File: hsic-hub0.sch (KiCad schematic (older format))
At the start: 26 parts

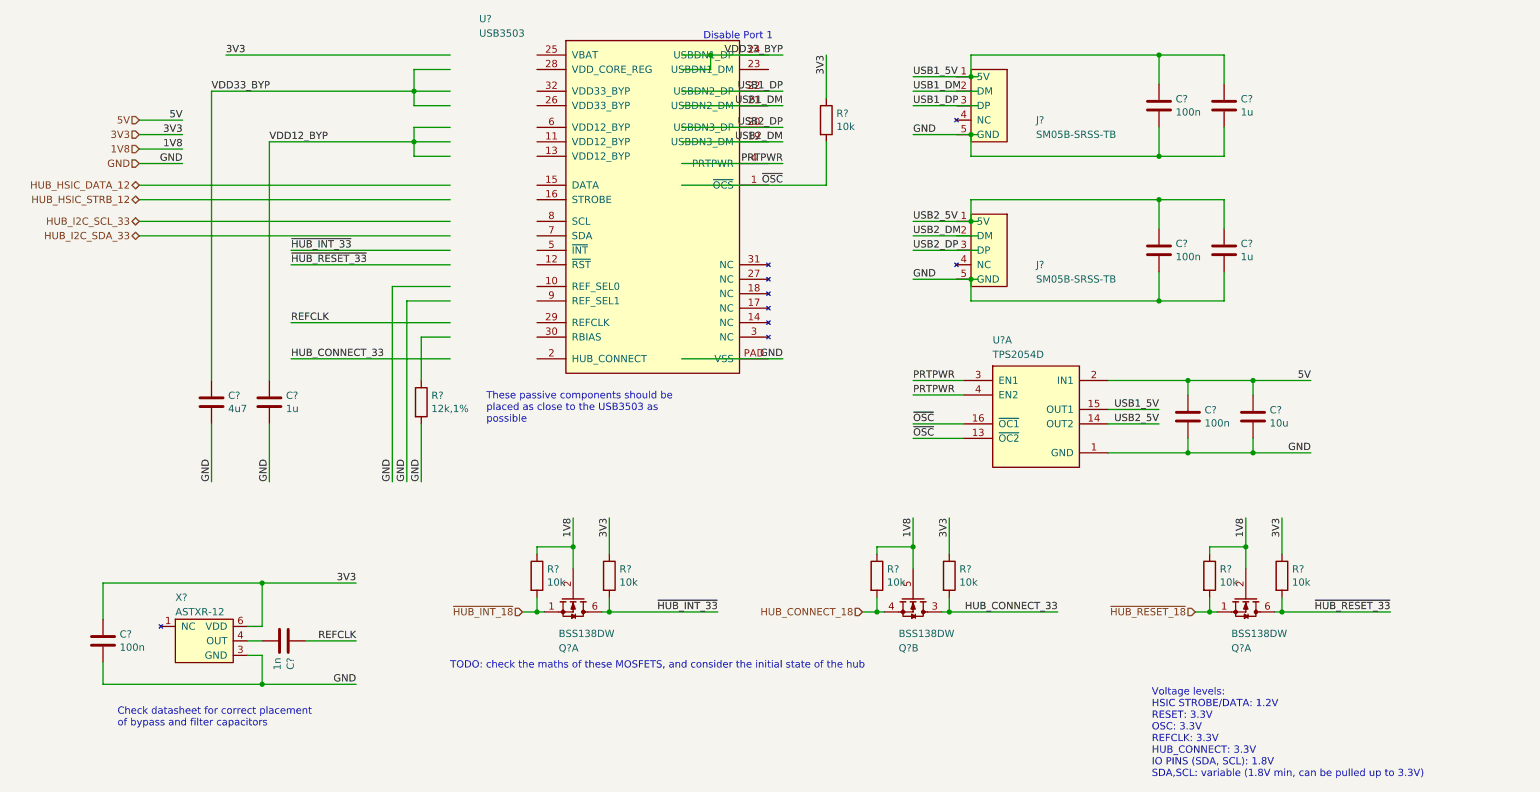
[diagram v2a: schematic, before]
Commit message: Added GPIO expander for hub signals.
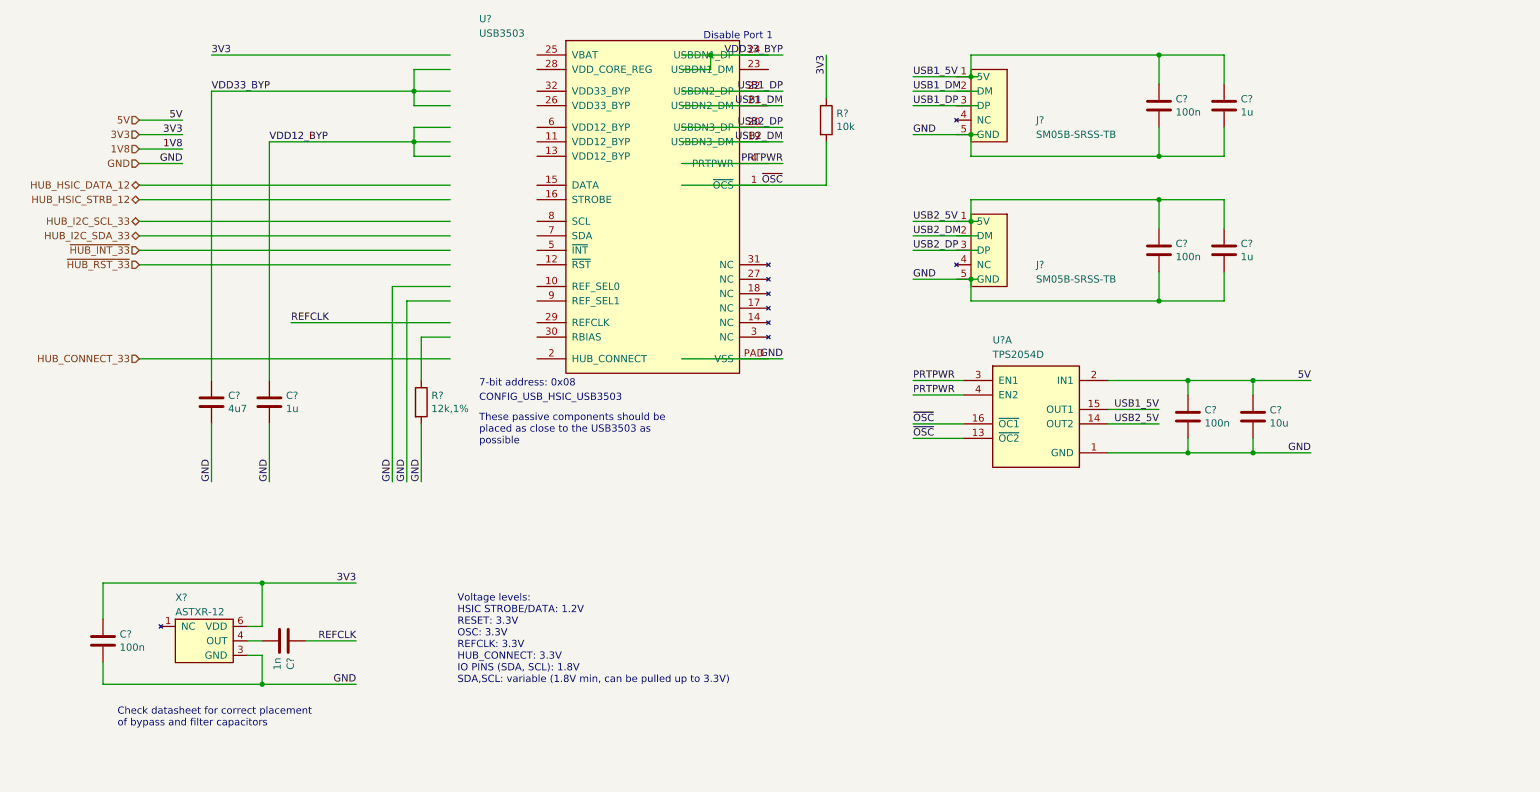
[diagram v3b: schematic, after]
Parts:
- removed Q? (x3): BSS138DW, symbol Drone:BSS138DW
- removed R? (x6): 10k, symbol Device:R
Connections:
- net labels added: ~HUB_RST_33
- net labels removed: HUB_CONNECT_18, ~HUB_INT_18, ~HUB_RESET_18, ~HUB_RESET_33
- wire segments 142 -> 109
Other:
- note added: "7-bit address: 0x08"
- note added: "CONFIG_USB_HSIC_USB3503"
- note removed: "TODO: check the maths of these MOSFETS, and consider the initial state of the hub"

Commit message: Use 0805 for all capacitors and resistors.
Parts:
- C? (x10): footprint (none) -> Capacitor_SMD:C_0805_2012Metric_Pad1.15x1.40mm_HandSolder; symbol Device:C -> Drone:CAP
- R? (x2): footprint (none) -> Resistor_SMD:R_0805_2012Metric_Pad1.15x1.40mm_HandSolder; symbol Device:R -> Drone:RES
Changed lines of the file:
@@
 	1400 2300 3550 2300
 $Comp
-L Device:C C?
+L Drone:CAP C?
 U 1 1 5E328065
 P 1150 5000
@@
 F 0 "C?" H 1265 5046 50  0000 L CNN
 F 1 "100n" H 1265 4955 50  0000 L CNN
-F 2 "" H 1188 4850 50  0001 C CNN
+F 2 "Capacitor_SMD:C_0805_2012Metric_Pad1.15x1.40mm_HandSolder" H 1188 4850 50  0001 C CNN
 F 3 "~" H 1150 5000 50  0001 C CNN
 	1    1150 5000
@@
 	5150 1700 5850 1700
 $Comp
-L Device:C C?
+L Drone:CAP C?
 U 1 1 5E332CF8
 P 8650 3450
@@
 F 0 "C?" H 8765 3496 50  0000 L CNN
 F 1 "100n" H 8765 3405 50  0000 L CNN
-F 2 "" H 8688 3300 50  0001 C CNN
+F 2 "Capacitor_SMD:C_0805_2012Metric_Pad1.15x1.40mm_HandSolder" H 8688 3300 50  0001 C CNN
 F 3 "~" H 8650 3450 50  0001 C CNN
 	1    8650 3450
@@
 	3150 2550 3550 2550
 $Comp
-L Device:C C?
+L Drone:CAP C?
 U 1 1 5E338829
 P 2400 5000
@@
 F 0 "C?" H 2515 5046 50  0000 L CNN
 F 1 "1n" H 2515 4955 50  0000 L CNN
-F 2 "" H 2438 4850 50  0001 C CNN
+F 2 "Capacitor_SMD:C_0805_2012Metric_Pad1.15x1.40mm_HandSolder" H 2438 4850 50  0001 C CNN
 F 3 "~" H 2400 5000 50  0001 C CNN
 	1    2400 5000
@@
 Disable Port 1
 $Comp
-L Device:C C?
+L Drone:CAP C?
 U 1 1 5E3408C5
 P 8450 1300
@@
 F 0 "C?" H 8565 1346 50  0000 L CNN
 F 1 "100n" H 8565 1255 50  0000 L CNN
-F 2 "" H 8488 1150 50  0001 C CNN
+F 2 "Capacitor_SMD:C_0805_2012Metric_Pad1.15x1.40mm_HandSolder" H 8488 1150 50  0001 C CNN
 F 3 "~" H 8450 1300 50  0001 C CNN
 	1    8450 1300
@@
 	7150 1500 7200 1500
 $Comp
-L Device:C C?
+L Drone:CAP C?
 U 1 1 5E3AC9C8
 P 8450 2300
@@
 F 0 "C?" H 8565 2346 50  0000 L CNN
 F 1 "100n" H 8565 2255 50  0000 L CNN
-F 2 "" H 8488 2150 50  0001 C CNN
+F 2 "Capacitor_SMD:C_0805_2012Metric_Pad1.15x1.40mm_HandSolder" H 8488 2150 50  0001 C CNN
 F 3 "~" H 8450 2300 50  0001 C CNN
 	1    8450 2300
@@
 ~OSC
 $Comp
-L Device:C C?
+L Drone:CAP C?
 U 1 1 5E4C4178
 P 8900 2300
@@
 F 0 "C?" H 9015 2346 50  0000 L CNN
 F 1 "1u" H 9015 2255 50  0000 L CNN
-F 2 "" H 8938 2150 50  0001 C CNN
+F 2 "Capacitor_SMD:C_0805_2012Metric_Pad1.15x1.40mm_HandSolder" H 8938 2150 50  0001 C CNN
 F 3 "~" H 8900 2300 50  0001 C CNN
 	1    8900 2300
@@
 $EndComp
 $Comp
-L Device:C C?
+L Drone:CAP C?
 U 1 1 5E4C557D
 P 8900 1300
@@
 F 0 "C?" H 9015 1346 50  0000 L CNN
 F 1 "1u" H 9015 1255 50  0000 L CNN
-F 2 "" H 8938 1150 50  0001 C CNN
+F 2 "Capacitor_SMD:C_0805_2012Metric_Pad1.15x1.40mm_HandSolder" H 8938 1150 50  0001 C CNN
 F 3 "~" H 8900 1300 50  0001 C CNN
 	1    8900 1300
@@
 	5150 1850 6150 1850
 $Comp
-L Device:R R?
+L Drone:RES R?
 U 1 1 5E301315
 P 6150 1400
@@
 F 0 "R?" H 6220 1446 50  0000 L CNN
 F 1 "10k" H 6220 1355 50  0000 L CNN
-F 2 "" V 6080 1400 50  0001 C CNN
+F 2 "Resistor_SMD:R_0805_2012Metric_Pad1.15x1.40mm_HandSolder" V 6080 1400 50  0001 C CNN
 F 3 "~" H 6150 1400 50  0001 C CNN
 	1    6150 1400
@@
 $EndComp
 $Comp
-L Device:C C?
+L Drone:CAP C?
 U 1 1 5E5A610D
 P 9100 3450
@@
 F 0 "C?" H 9215 3496 50  0000 L CNN
 F 1 "10u" H 9215 3405 50  0000 L CNN
-F 2 "" H 9138 3300 50  0001 C CNN
+F 2 "Capacitor_SMD:C_0805_2012Metric_Pad1.15x1.40mm_HandSolder" H 9138 3300 50  0001 C CNN
 F 3 "~" H 9100 3450 50  0001 C CNN
 	1    9100 3450
@@
 These passive components should be\nplaced as close to the USB3503 as\npossible\n
 $Comp
-L Device:C C?
+L Drone:CAP C?
 U 1 1 5E427B4C
 P 1900 3350
@@
 F 0 "C?" H 2015 3396 50  0000 L CNN
 F 1 "4u7" H 2015 3305 50  0000 L CNN
-F 2 "" H 1938 3200 50  0001 C CNN
+F 2 "Capacitor_SMD:C_0805_2012Metric_Pad1.15x1.40mm_HandSolder" H 1938 3200 50  0001 C CNN
 F 3 "~" H 1900 3350 50  0001 C CNN
 	1    1900 3350
@@
 $EndComp
 $Comp
-L Device:C C?
+L Drone:CAP C?
 U 1 1 5E42226D
 P 2300 3350
@@
 F 0 "C?" H 2415 3396 50  0000 L CNN
 F 1 "1u" H 2415 3305 50  0000 L CNN
-F 2 "" H 2338 3200 50  0001 C CNN
+F 2 "Capacitor_SMD:C_0805_2012Metric_Pad1.15x1.40mm_HandSolder" H 2338 3200 50  0001 C CNN
 F 3 "~" H 2300 3350 50  0001 C CNN
 	1    2300 3350
@@
 	3250 3900 3250 2650
 $Comp
-L Device:R R?
+L Drone:RES R?
 U 1 1 5E32A1DA
 P 3350 3350
@@
 F 0 "R?" H 3420 3396 50  0000 L CNN
 F 1 "12k,1%" H 3420 3305 50  0000 L CNN
-F 2 "" V 3280 3350 50  0001 C CNN
+F 2 "Resistor_SMD:R_0805_2012Metric_Pad1.15x1.40mm_HandSolder" V 3280 3350 50  0001 C CNN
 F 3 "~" H 3350 3350 50  0001 C CNN
 	1    3350 3350

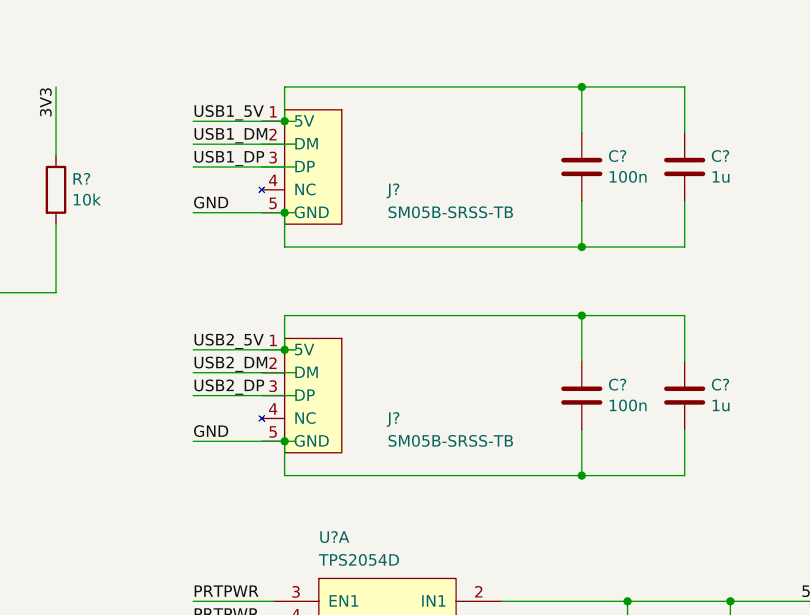
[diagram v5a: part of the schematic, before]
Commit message: Update the LEDs and resistor values. Add TELEM2 connector for Pixhawk.
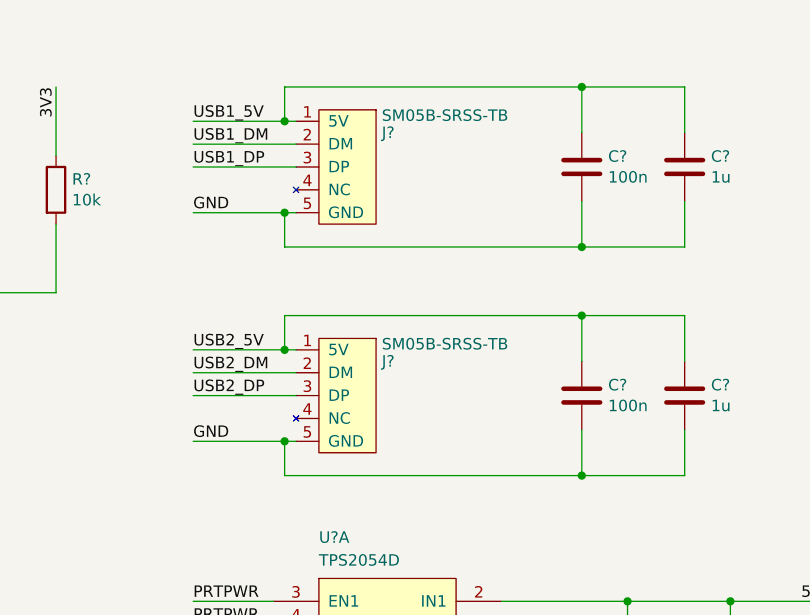
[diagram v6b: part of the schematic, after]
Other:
- moved on the sheet: J?
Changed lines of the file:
@@
 L Drone:SM05B-SRSS-TB J?
 U 1 1 5E385FFC
-P 7400 1050
+P 7550 1050
 AR Path="/5E2EDC4D/5E385FFC" Ref="J?"  Part="1"
 AR Path="/5E349830/5E385FFC" Ref="J?"  Part="1"
-F 0 "J?" H 7200 700 50  0000 R CNN
-F 1 "SM05B-SRSS-TB" H 7200 600 50  0000 R CNN
-F 2 "Drone:SM05B-SRSS-TB" H 7250 1300 50  0001 L CNN
-F 3 "" H 7400 1050 50  0001 C CNN
-	1    7400 1050
+F 0 "J?" H 7525 950 50  0000 R CNN
+F 1 "SM05B-SRSS-TB" H 7525 1025 50  0000 R CNN
+F 2 "Drone:SM05B-SRSS-TB" H 7400 1300 50  0001 L CNN
+F 3 "" H 7550 1050 50  0001 C CNN
+	1    7550 1050
 	-1   0    0    -1
 $EndComp
@@
 L Drone:SM05B-SRSS-TB J?
 U 1 1 5E3AC9C2
-P 7400 2050
+P 7550 2050
 AR Path="/5E2EDC4D/5E3AC9C2" Ref="J?"  Part="1"
 AR Path="/5E349830/5E3AC9C2" Ref="J?"  Part="1"
-F 0 "J?" H 7200 1700 50  0000 R CNN
-F 1 "SM05B-SRSS-TB" H 7200 1600 50  0000 R CNN
-F 2 "Drone:SM05B-SRSS-TB" H 7250 2300 50  0001 L CNN
-F 3 "" H 7400 2050 50  0001 C CNN
-	1    7400 2050
+F 0 "J?" H 7525 1950 50  0000 R CNN
+F 1 "SM05B-SRSS-TB" H 7525 2025 50  0000 R CNN
+F 2 "Drone:SM05B-SRSS-TB" H 7400 2300 50  0001 L CNN
+F 3 "" H 7550 2050 50  0001 C CNN
+	1    7550 2050
 	-1   0    0    -1
 $EndComp

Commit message: Minor fixes.
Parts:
- removed C? (x2): 1u, Capacitor_SMD:C_0805_2012Metric_Pad1.15x1.40mm_HandSolder, symbol Drone:CAP
- added C?: 100n, Capacitor_SMD:C_0805_2012Metric_Pad1.15x1.40mm_HandSolder, symbol Drone:CAP
- added R?: DNP, Resistor_SMD:R_0805_2012Metric_Pad1.15x1.40mm_HandSolder, symbol Drone:RES
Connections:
- net labels removed: 1V8
- wire segments 109 -> 107
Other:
- moved on the sheet: C?, J?, R?, U?, U?A
